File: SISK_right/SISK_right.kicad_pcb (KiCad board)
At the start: 2 copper layers, 194.5 x 121.8 mm, 90 parts, among them J1 OLED_128x32, J2 Battery Conn, SW1 "6", SW10 "Z", SW11 "U", SW12 "I", SW13 "O", SW14 "P", SW15 "Ü", SW16 "*", SW17 "Enter", SW18 "Del", SW19 "H", SW2 "7", SW20 "J", SW21 "K", SW22 "L", SW23 "Ö", SW24 "Ä", SW25 "'", SW26 "PGUP", SW27 "N", SW28 "M", SW29 ";", SW3 "8", SW30 ":", SW31 "-", SW32 "shift_R", SW33 "UP", SW34 "PGDOWN", SW35 "SPACE_R", SW36 "Alt", SW37 FN, SW38 "Ctrl", SW39 "Left", SW4 "9", SW40 "Down", SW41 "Right", SW5 "0", SW6 "ß", SW7 "`", SW8 "Backspace", SW9 "^", U1 Nice_Nano_V2

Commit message: up
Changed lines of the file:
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@@
 		(at 80.835 47.465 180)
 		(property "Reference" "J1"
-			(at 7.75 10 360)
+			(at 7.75 10 0)
 			(layer "F.SilkS")
 			(hide yes)
@@
 		)
 		(property "Value" "OLED_128x32"
-			(at 5.75 5.75 360)
+			(at 5.75 5.75 0)
 			(layer "F.Fab")
 			(hide yes)
@@
 		)
 		(property "Footprint" "ScottoKeebs_Components:OLED_128x32"
-			(at 0 0 360)
+			(at 0 0 0)
 			(layer "F.Fab")
 			(hide yes)
@@
 		)
 		(property "Datasheet" ""
-			(at 0 0 360)
+			(at 0 0 0)
 			(layer "F.Fab")
 			(hide yes)
@@
 		)
 		(property "Description" ""
-			(at 0 0 360)
+			(at 0 0 0)
 			(layer "F.Fab")
 			(hide yes)
@@
 		)
 		(fp_text user "GND"
-			(at -6.35 5.461 360)
+			(at -6.35 5.461 0)
 			(layer "B.SilkS")
 			(hide yes)
@@
 		)
 		(fp_text user "D7"
-			(at 6.35 5.461 360)
+			(at 6.35 5.461 0)
 			(layer "B.SilkS")
 			(hide yes)
@@
 	)
 	(gr_text "OLED"
-		(at 46.785 44.89 90)
+		(at 78.06 44.34 90)
 		(layer "F.SilkS")
 		(effects
@@
 	)
 	(gr_text "VCC"
-		(at 40.91 45.54 0)
+		(at 80.21 40.84 0)
 		(layer "F.SilkS")
 		(effects
@@
 	)
 	(gr_text "GND\n"
-		(at 43.01 48.865 0)
+		(at 80.235 38.265 0)
 		(layer "F.SilkS")
 		(effects

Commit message: changes after first review
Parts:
- added REF02: MountingHole_3.2mm_M3_ISO7380, MountingHole:MountingHole_3.2mm_M3_ISO7380, F.Cu at (138.2, 73.8)
- added REF05: MountingHole_3.2mm_M3_ISO7380, MountingHole:MountingHole_3.2mm_M3_ISO7380, F.Cu at (157.3, 132.3)
- renumbered REF** to REF01, REF** to REF03, REF** to REF04, REF** to REF06
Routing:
- net /COL8: track 259.9 -> 271.3 mm
- net /COL7: track 229.2 -> 233.1 mm
- net /COL0: track 120.9 -> 124.8 mm
- net /COL2: track 159.1 -> 156.9 mm
- net Net-(D12-A): track 15.0 -> 12.8 mm
- net /COL4: track 184.4 -> 186.2 mm
- net /COL3: track 158.6 -> 160.2 mm
- net Net-(D6-A): track 17.3 -> 18.7 mm
- net Net-(D31-A): track 13.7 -> 15.0 mm
- net Net-(D34-A): track 12.4 -> 13.5 mm
- net Net-(D4-A): track 12.4 -> 13.5 mm
- net Net-(D29-A): track 12.4 -> 13.5 mm
- net Net-(D19-A): track 12.4 -> 13.5 mm
- net Net-(D39-A): track 12.4 -> 13.5 mm
- net Net-(D9-A): track 12.4 -> 13.5 mm
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
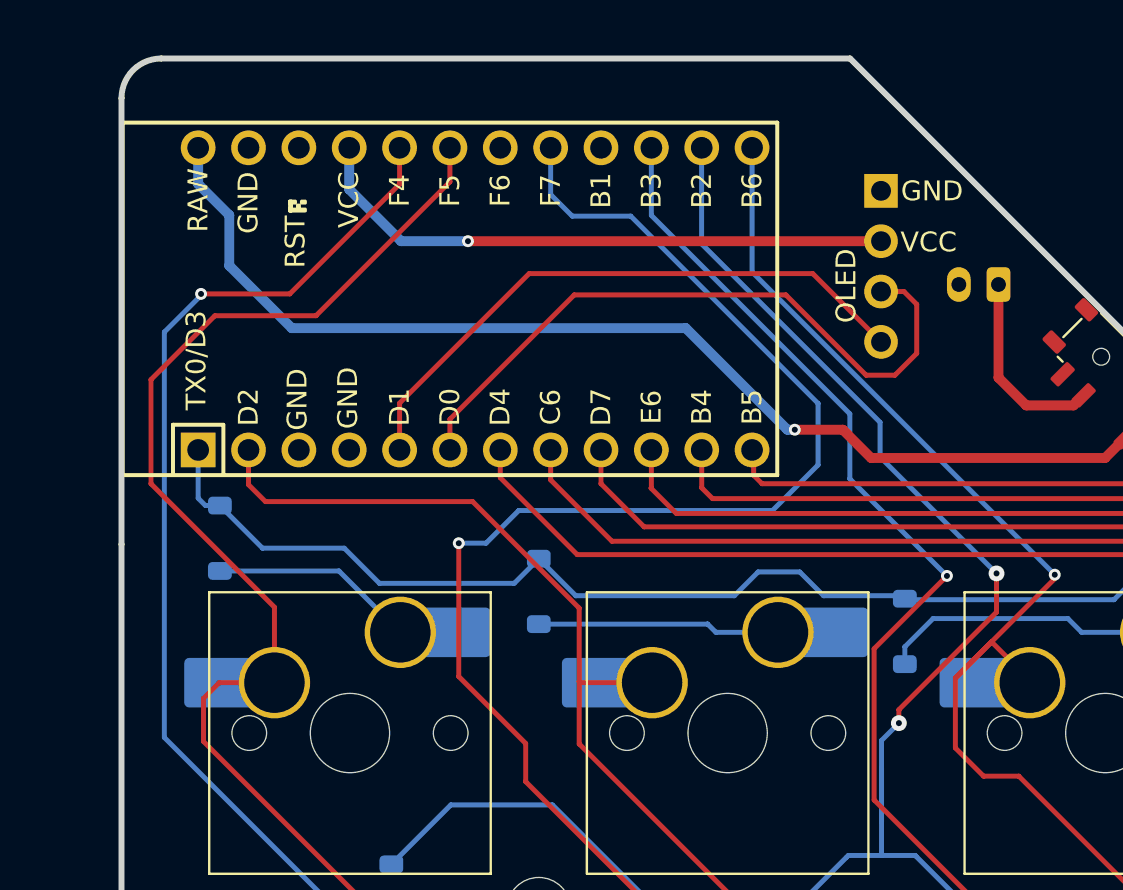
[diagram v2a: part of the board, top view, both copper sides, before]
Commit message: changed nice nano footprint
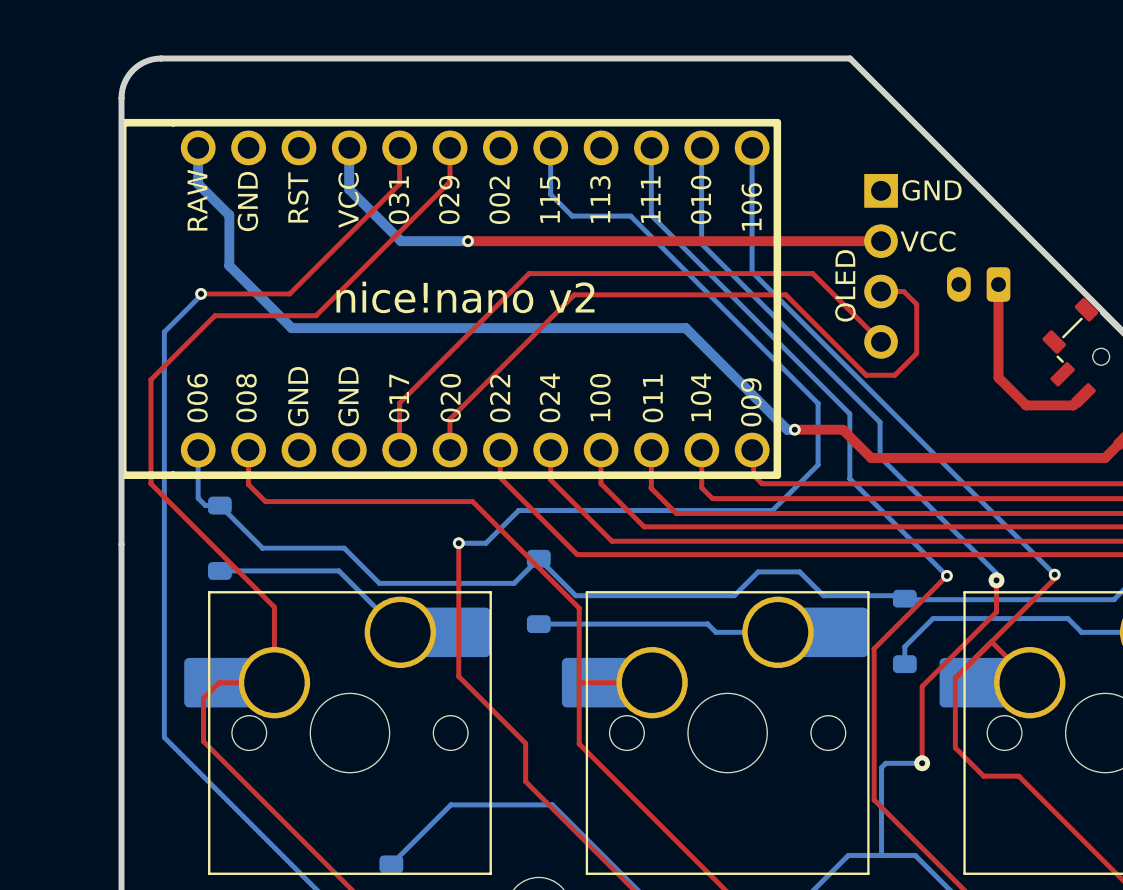
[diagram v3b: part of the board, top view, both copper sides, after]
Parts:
- U1: footprint ScottoKeebs_MCU:Arduino_Pro_Micro -> nice-nano-kicad-master:nice_nano
- turned U1 to 0 degrees
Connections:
- SW-ONOFF-01 pad MP: (no net) -> GND
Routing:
- net /ROW1: track 222.1 -> 223.1 mm
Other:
- board text added: "009"
- board text added: "106"

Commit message: added some text and alternative header for Power Switch
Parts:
- added J3: alternative on/off SW (wired), Connector_PinHeader_2.54mm:PinHeader_1x02_P2.54mm_Vertical, F.Cu at (82.2, 39.9)
- SW-ONOFF-01: value ~ -> onboard ON/OFF SW
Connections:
- SW-ONOFF-01 pad MP: GND -> (no net)
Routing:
- net Net-(J3-Pin_1): track 56.3 -> 68.9 mm
- net +3.3V: track 9.85 -> 12.5 mm
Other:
- board text added: "designed by d4ve October 2024 Rev 1.0"
